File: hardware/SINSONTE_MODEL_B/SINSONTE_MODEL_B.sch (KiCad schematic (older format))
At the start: 35 parts, among them J1 BAT, J10 Conn_01x02_Male, J11 Conn_01x02_Male, J12 Conn_01x02_Male, J13 Conn_01x02_Male, J14 Conn_01x02_Male, J15 Conn_01x02_Male, J16 Conn_01x02_Male, J17 Conn_01x02_Male, J18 Conn_01x02_Male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

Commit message: shrinkikng in process
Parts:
- added J19: Conn_01x06_Male, Connector_PinHeader_2.54mm:PinHeader_1x06_P2.54mm_Vertical, symbol Connector:Conn_01x06_Male
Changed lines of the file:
@@
 Text Notes 9750 5150 0    50   ~ 0
 PROTO AREA
+$Comp
+L Connector:Conn_01x06_Male J19
+U 1 1 618C77ED
+P 10200 4300
+F 0 "J19" H 10308 4681 50  0000 C CNN
+F 1 "Conn_01x06_Male" H 10308 4590 50  0000 C CNN
+F 2 "Connector_PinHeader_2.54mm:PinHeader_1x06_P2.54mm_Vertical" H 10200 4300 50  0001 C CNN
+F 3 "~" H 10200 4300 50  0001 C CNN
+	1    10200 4300
+	1    0    0    -1
+$EndComp
 $EndSCHEMATC

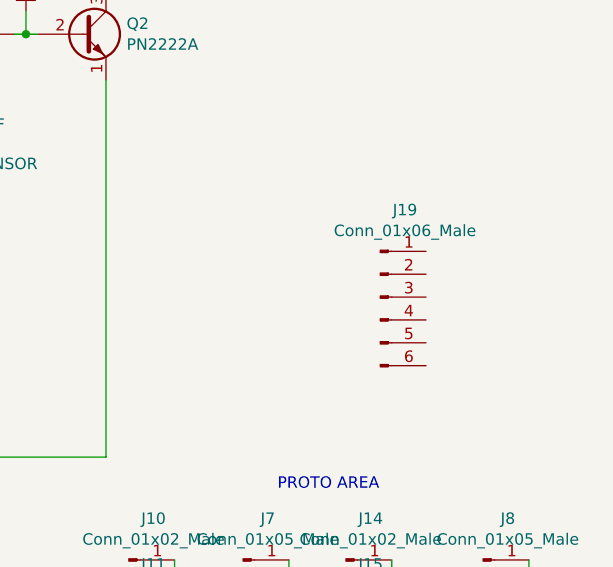
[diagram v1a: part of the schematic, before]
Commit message: shrinkikng finished
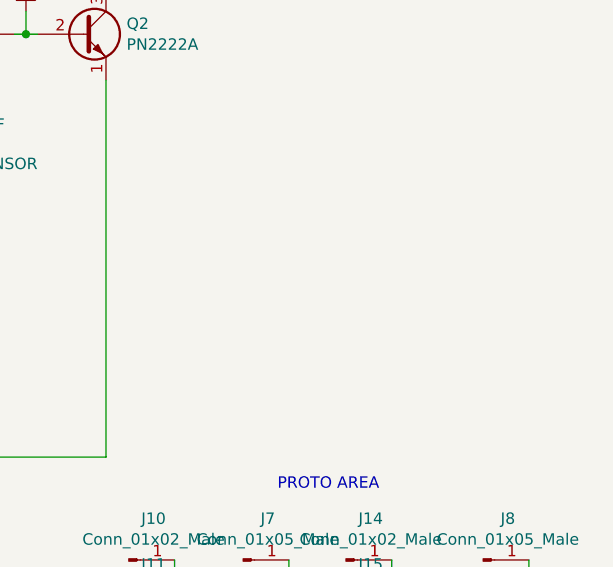
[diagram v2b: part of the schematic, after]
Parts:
- removed J19: Conn_01x06_Male, Connector_PinHeader_2.54mm:PinHeader_1x06_P2.54mm_Vertical, symbol Connector:Conn_01x06_Male
- BT1: footprint Battery:BatteryHolder_Keystone_2462_2xAA -> Connector_PinHeader_2.54mm:PinHeader_1x02_P2.54mm_Vertical
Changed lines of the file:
@@
 F 0 "BT1" H 2050 3000 50  0000 L CNN
 F 1 "Battery_Cell" H 1950 2800 50  0000 L CNN
-F 2 "Battery:BatteryHolder_Keystone_2462_2xAA" V 2500 2910 50  0001 C CNN
+F 2 "Connector_PinHeader_2.54mm:PinHeader_1x02_P2.54mm_Vertical" V 2500 2910 50  0001 C CNN
 F 3 "~" V 2500 2910 50  0001 C CNN
 	1    2500 2850
@@
 Text Notes 9750 5150 0    50   ~ 0
 PROTO AREA
-$Comp
-L Connector:Conn_01x06_Male J19
-U 1 1 618C77ED
-P 10200 4300
-F 0 "J19" H 10308 4681 50  0000 C CNN
-F 1 "Conn_01x06_Male" H 10308 4590 50  0000 C CNN
-F 2 "Connector_PinHeader_2.54mm:PinHeader_1x06_P2.54mm_Vertical" H 10200 4300 50  0001 C CNN
-F 3 "~" H 10200 4300 50  0001 C CNN
-	1    10200 4300
-	1    0    0    -1
-$EndComp
 $EndSCHEMATC
